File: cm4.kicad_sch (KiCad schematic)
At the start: 34 parts, among them Q1 MMBT2222AM3T5G, U3 PCA9671BS,118

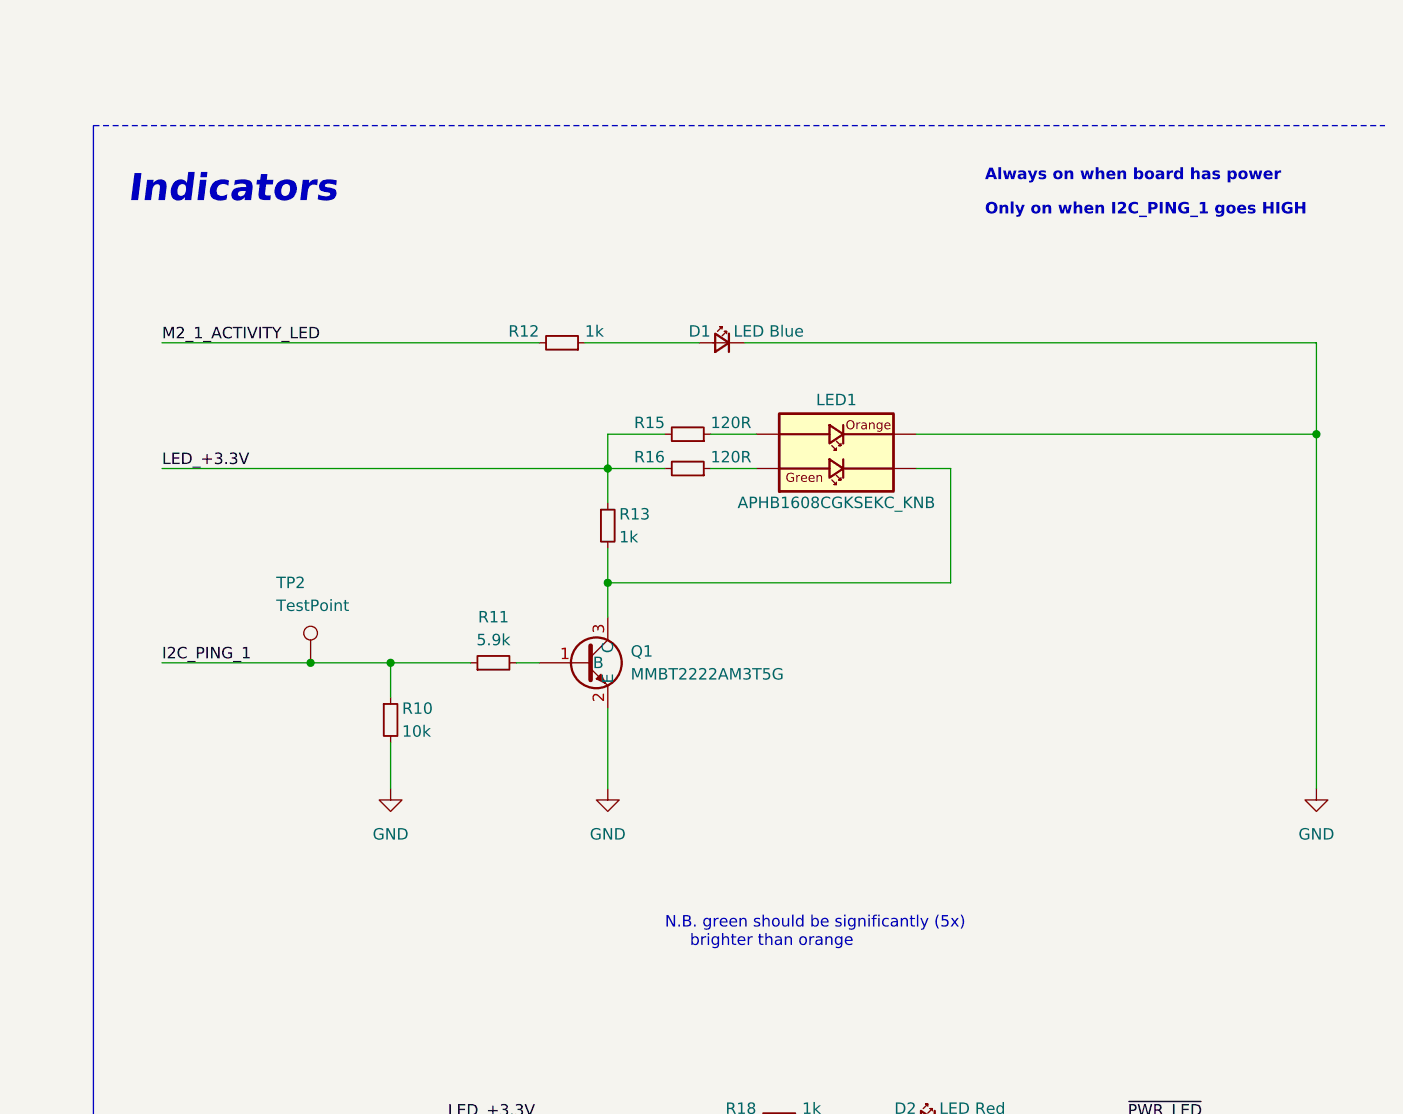
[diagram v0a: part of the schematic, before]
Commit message: fixed I2C ping indicator
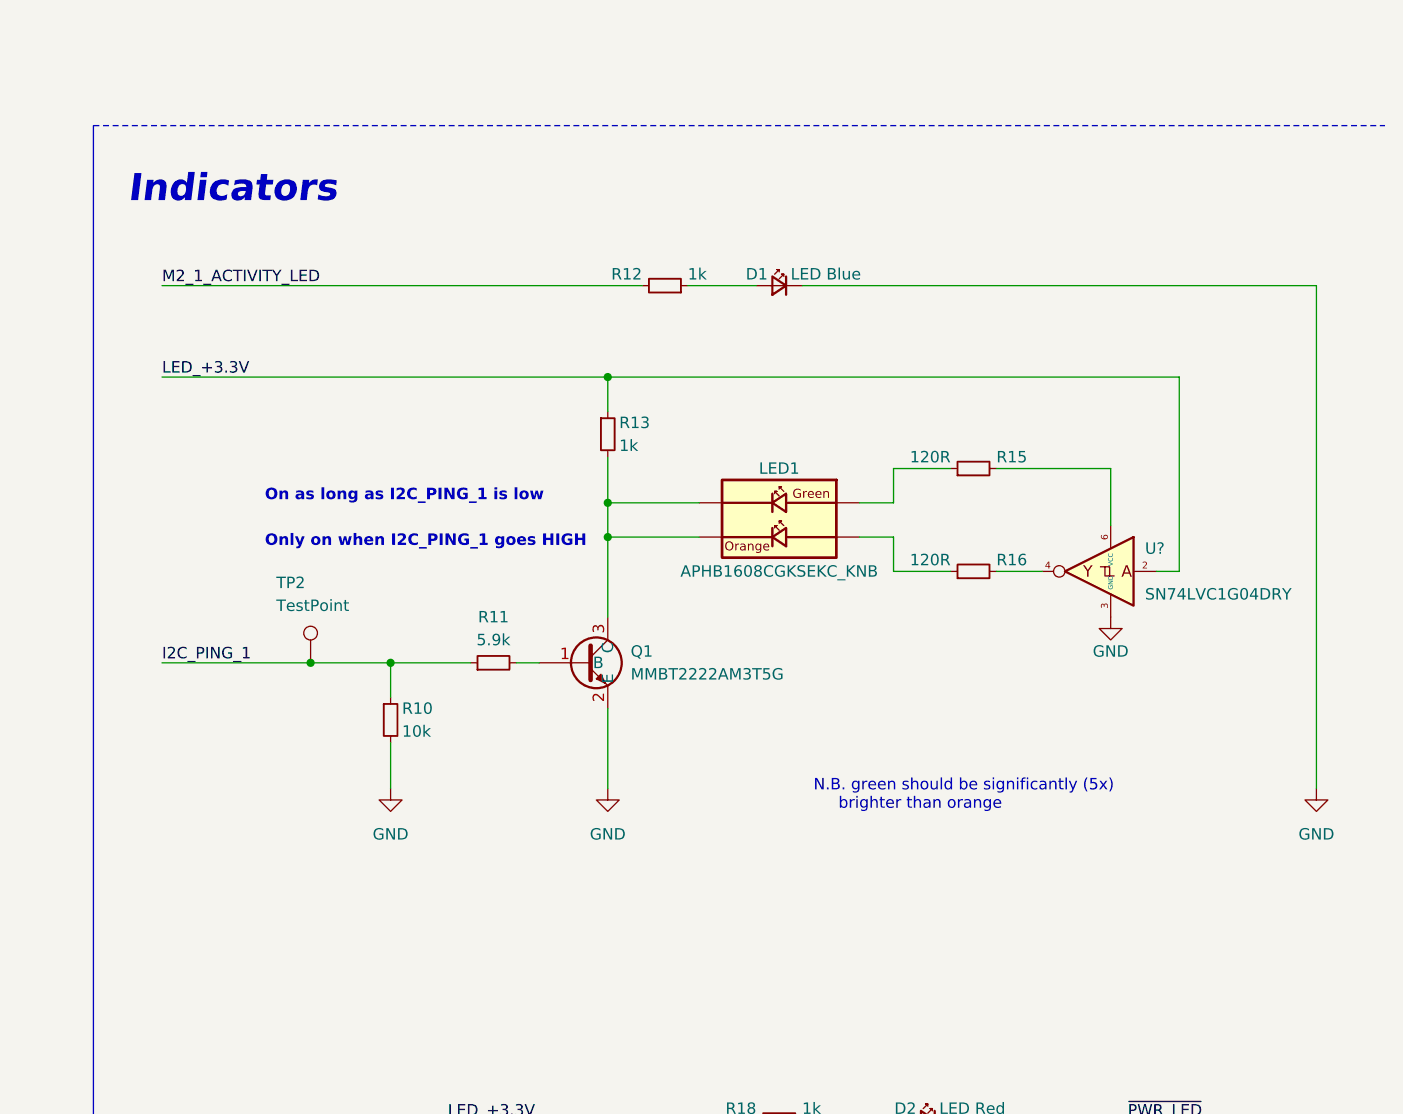
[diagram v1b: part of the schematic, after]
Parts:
- added U?: SN74LVC1G04DRY, Inverter_SMD_TI:PSON50P145X100X60-6N-DRY0006A, symbol Inverter_SMD_TI:SN74LVC1G04DRY
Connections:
- net CM4_+3.3V: now also U?.2; no longer R15.2, R16.2
- net GND: now also U?.3 (GND); no longer LED1.4
- net at R16.1: now also LED1.3; no longer LED1.1
- net at LED1.2, Q1.3 (C), R13.2: now also LED1.4
- net at R15.1: now also LED1.1; no longer LED1.3
- new net: R16.2, U?.4
- new net: R15.2, U?.6 (VCC)
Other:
- note added: "On as long as I2C_PING_1 is low"
- note removed: "Always on when board has power"
- moved on the sheet: D1, LED1, R12, R13, R15, R16

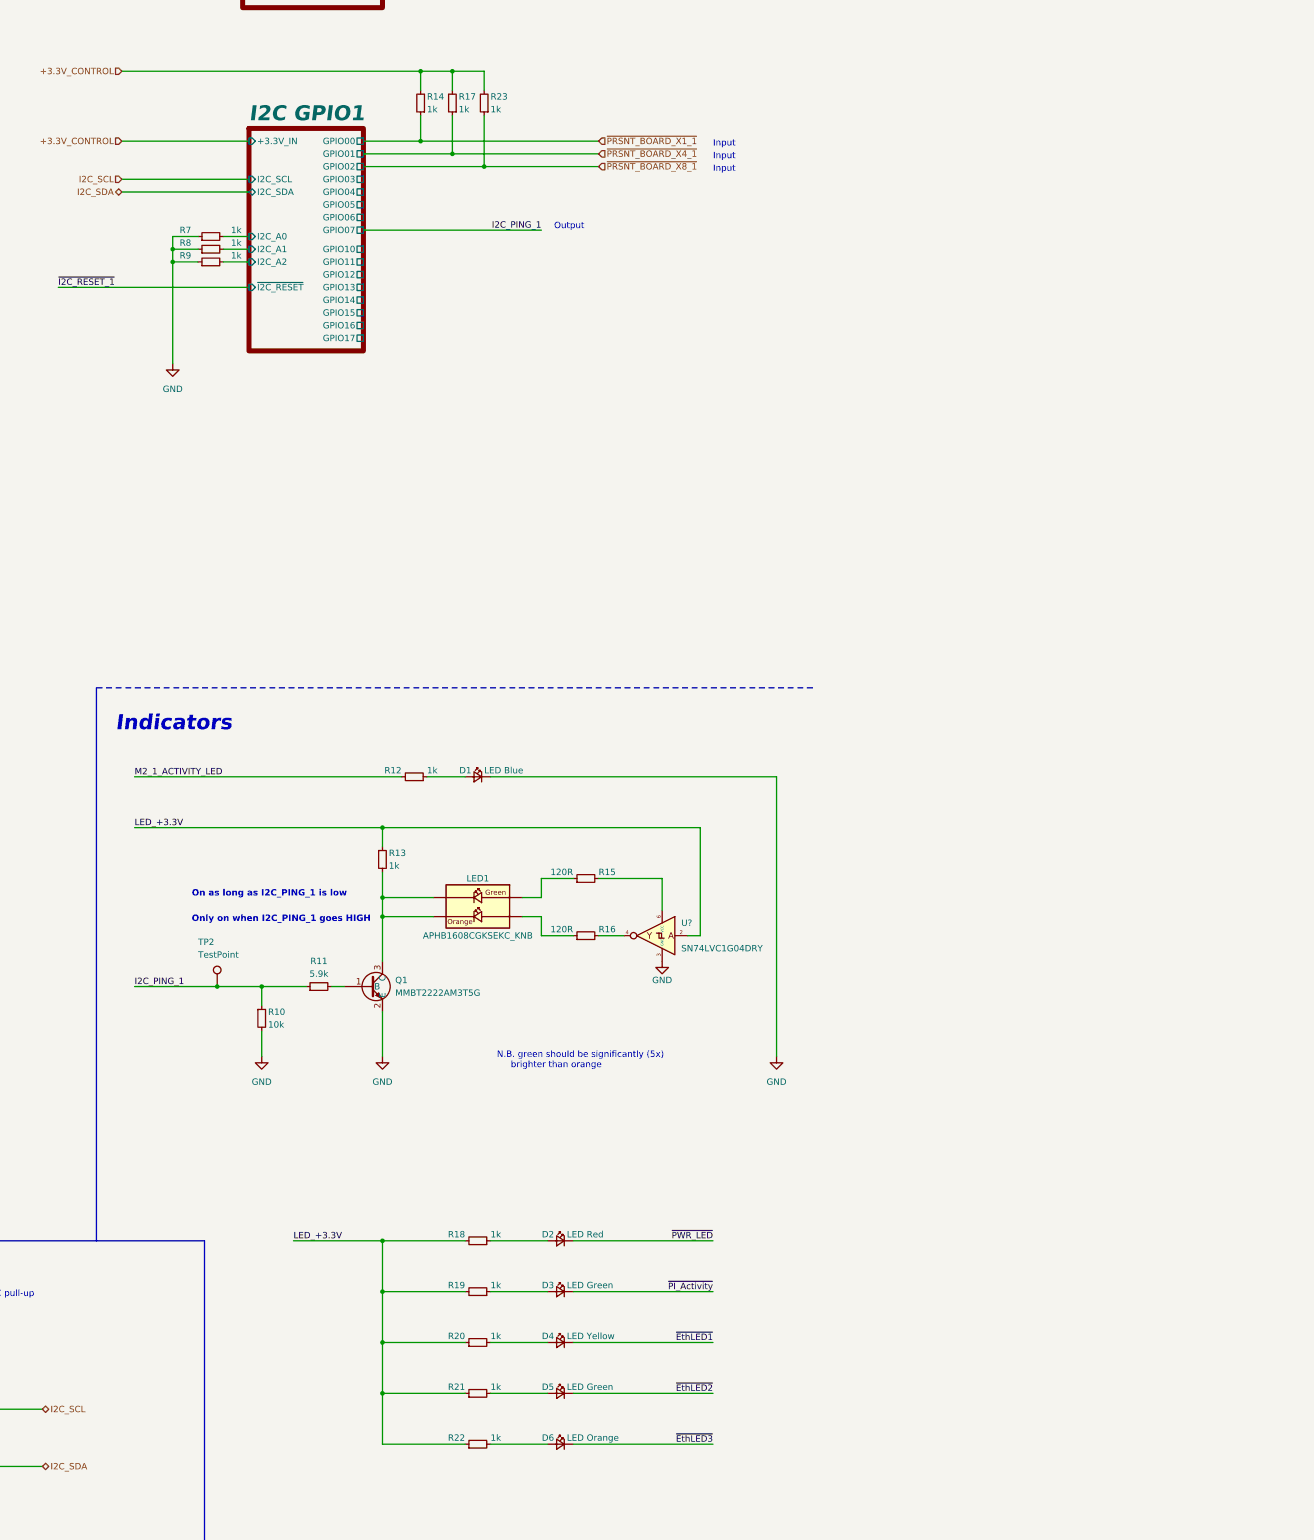
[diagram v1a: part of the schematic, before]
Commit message: added ti buffer lib
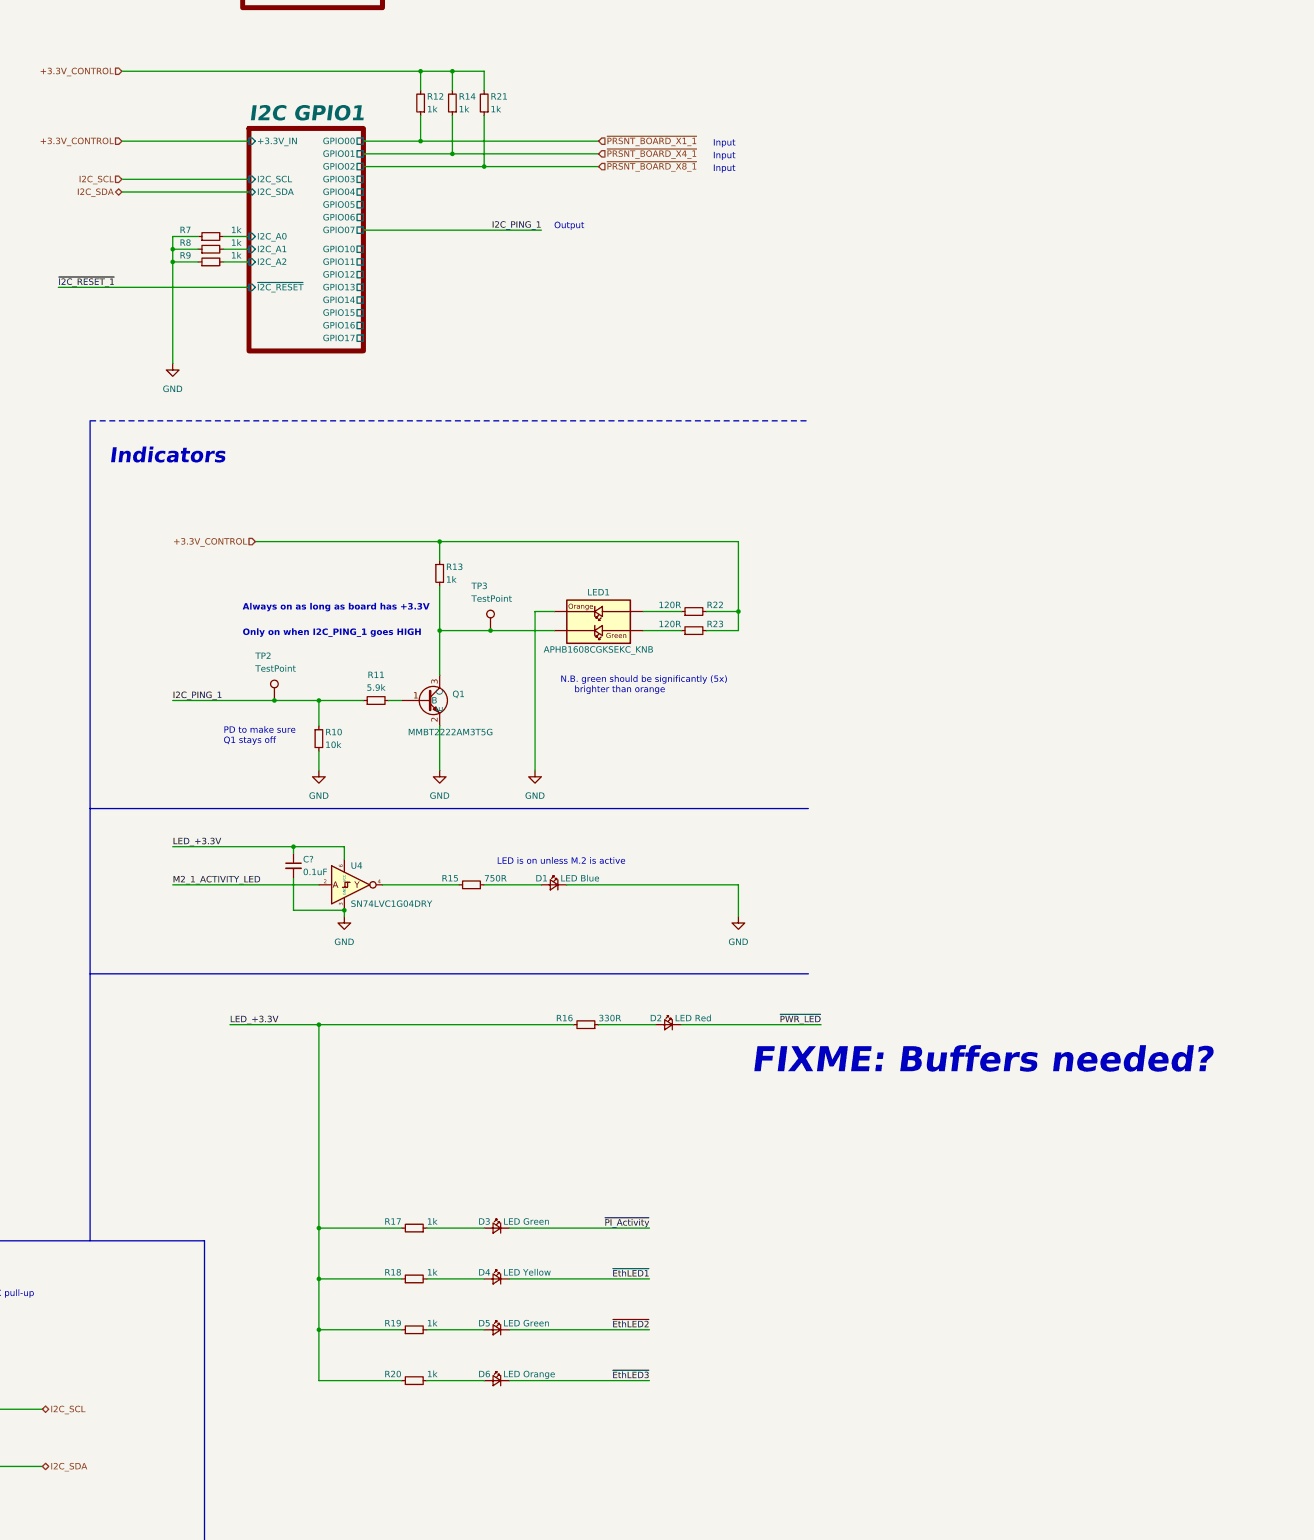
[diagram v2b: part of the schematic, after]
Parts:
- removed U?: SN74LVC1G04DRY, Inverter_SMD_TI:PSON50P145X100X60-6N-DRY0006A, symbol Inverter_SMD_TI:SN74LVC1G04DRY
- added C?: 0.1uF, Capacitor_SMD:C_0402_1005Metric, symbol Device:C_Small
- added TP3: TestPoint, TestPoint:TestPoint_Pad_D1.0mm, symbol Connector:TestPoint
- added U4: SN74LVC1G04DRY, Inverter_SMD_TI:PSON50P145X100X60-6N-DRY0006A, symbol Inverter_SMD_TI:SN74LVC1G04DRY
- R15: renamed from R12; value 1k -> 750R
- R16: renamed from R18; value 1k -> 330R
- renumbered R14 to R12, R17 to R14, R19 to R17, R20 to R18, R21 to R19, R22 to R20, R23 to R21, R15 to R22, R16 to R23
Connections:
- net +3.3V_CONTROL: now also R13.1, R22.2, R23.2
- net CM4_+3.3V: now also C?.1, U4.6 (VCC); no longer R13.1
- net GND: now also LED1.4, C?.2, U4.3 (GND)
- net M2_1_ACTIVITY_LED: now also U4.2; no longer R15.2
- net at R23.1: now also LED1.1; no longer LED1.3
- net at R22.1: now also LED1.3; no longer LED1.1
- net at LED1.2, Q1.3 (C), R13.2: now also TP3.1; no longer LED1.4
- new net: R15.2, U4.4
- new net: U4.1 (NC), U4.5 (NC)
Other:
- note added: "Always on as long as board has +3.3V"
- note added: "FIXME: Buffers needed?"
- note added: "LED is on unless M.2 is active"
- note added: "PD to make sure Q1 stays off"
- note removed: "On as long as I2C_PING_1 is low"
- moved on the sheet: D1, D2, D3, D4, D5, D6, LED1, Q1, R10, R11, R13, R15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

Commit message: more indicator fixes
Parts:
- added TP? (x6): TestPoint, TestPoint:TestPoint_Pad_D1.0mm, symbol Connector:TestPoint
- added U?: SN74LVC1G07DRY, Buffer_SMD_TI:PSON50P145X100X60-6N-DRY0006A, symbol Buffer_SMD_TI:SN74LVC1G07DRY
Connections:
- net CM4_+3.3V: now also U?.6 (VCC)
- net GND: now also U?.3 (GND)
- net ~{EthLED1}: now also TP?.1
- net ~{EthLED2}: now also TP?.1
- net ~{EthLED3}: now also TP?.1
- net ~{PI_Activity}: now also TP?.1
- net ~{PWR_LED}: now also U?.2; no longer D2.1 (K)
- net at R15.2, U4.4: now also TP?.1
- new net: U?.1 (NC), U?.5 (NC)
- new net: D2.1 (K), TP?.1, U?.4
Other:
- note added: "Indicators - CM4"
- note added: "Indicators - I2C"
- note added: "Indicators - M.2"
- note removed: "FIXME: Buffers needed?"
- note removed: "Indicators"
- moved on the sheet: C?, D1, D2, R15, R16, U4

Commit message: initial integration of i2c arbiter
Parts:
- added C8, C?: 0.1uF, Capacitor_SMD:C_0402_1005Metric, symbol Device:C_Small
- added C?: 10uF, Capacitor_SMD:C_0402_1005Metric, symbol Device:C_Small
- added R? (x4): 1k, symbol Device:R_Small
- added R? (x2): 5.1k, Resistor_SMD:R_0402_1005Metric, symbol Device:R_Small
- added U?: PCA9641BSHP, Interface_I2C_NXP:SOT758-1_HVQFN-16_3x3mm_P0.5mm_EP1.75x1.75mm_NXP, symbol Interface_I2C_NXP:PCA9641BSHP
- gave numbers to parts that had none: 8
- renumbered D2 to D1, D3 to D2, D4 to D3, D5 to D4, D6 to D5, D1 to D6, R16 to R12, R17 to R13, R18 to R14, R19 to R15, R20 to R16, R12 to R17, R13 to R18, R14 to R19, R15 to R20, TP3 to TP4
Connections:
- net +3.3V_CONTROL: now also C?.1, C?.1, R?.2, R?.2, U?.14 (VDD)
- net GND: now also C8.2, C?.2, C?.2, R?.1, R?.1, R?.1, R?.1, U?.6 (VSS)
- net I2C_SCL: now also U?.11 (SCL_SLAVE)
- net I2C_SDA: now also U?.12 (SDA_SLAVE)
- net at D1.1 (K), TP5.1, U5.4: now also C8.1
- new net: R?.2, U?.10 (AD3)
- new net: R?.2, U?.7 (AD0)
- new net: R?.2, U?.8 (AD1)
- new net: R?.2, U?.9 (AD2)
- new net BACKPLANE_I2C_SCL: U?.1 (SCL_MST0)
- new net BACKPLANE_I2C_SDA: U?.16 (SDA_MST0)
- new net CM4_I2C_SCL: R?.1, U?.3 (SCL_MST1)
- new net CM4_I2C_SDA: R?.1, U?.4 (SDA_MST1)
- no-connect marks 29 -> 33
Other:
- note added: "CM4 I2C bus"
- note removed: "FIXME: Need arbiter"
- note removed: "Local I2C bus"
- moved on the sheet: R5, R6

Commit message: refresh
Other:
- note added: "Green: Only on when I2C_PING_1 goes HIGH"
- note added: "Orange: Always on as long as board has +3.3V_CONTROL"
- note removed: "Always on as long as board has +3.3V"
- note removed: "Only on when I2C_PING_1 goes HIGH"
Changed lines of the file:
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@@
     (effects (font (size 1.27 1.27)) (justify left bottom))
   )
-  (text "Always on as long as board has +3.3V" (at 464.82 199.39 0)
+  (text "Orange: Always on as long as board has +3.3V_CONTROL"
+    (at 445.77 199.39 0)
     (effects (font (size 1.27 1.27) (thickness 0.254) bold) (justify left bottom))
   )
@@
     (effects (font (size 1.27 1.27)) (justify left bottom))
   )
-  (text "Only on when I2C_PING_1 goes HIGH" (at 464.82 204.47 0)
+  (text "Green: Only on when I2C_PING_1 goes HIGH" (at 445.77 204.47 0)
     (effects (font (size 1.27 1.27) (thickness 0.254) bold) (justify left bottom))
   )

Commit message: refresh
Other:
- note added: "FIXME: USB hub and Coral TPU?"
- note added: "FIXME: check all pullups"
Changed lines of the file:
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@@
     (effects (font (size 1.27 1.27)) (justify right bottom))
+  )
+  (text "FIXME: check all pullups" (at 605.79 170.18 0)
+    (effects (font (size 5 5) (thickness 1) bold italic) (justify left bottom))
   )
   (text "Input" (at 347.98 381 0)
@@
     (effects (font (size 3 3)) (justify left bottom))
   )
+  (text "FIXME: USB hub and Coral TPU?" (at 605.79 193.04 0)
+    (effects (font (size 5 5) (thickness 1) bold italic) (justify left bottom))
+  )
   (text "Input" (at 558.8 109.22 0)
